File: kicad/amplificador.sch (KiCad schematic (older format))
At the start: 80 parts, among them J1 Screw_Terminal_01x01, J10 Conn_01x01_Male, J11 Conn_01x01_Male, J12 Conn_01x01_Male, J13 Conn_01x01_Male, J14 Screw_Terminal_01x01, J16 Screw_Terminal_01x01, J17 Screw_Terminal_01x01, J18 Conn_01x01_Male, J19 Conn_01x01_Male, J2 Conn_01x01_Male, J3 Conn_01x01_Male, J4 Conn_01x01_Male, J5 Conn_01x01_Male, J6 Conn_01x01_Male, J7 Screw_Terminal_01x01, J8 Screw_Terminal_01x01, J9 Conn_01x01_Male, Q1 MPSA92, Q10 MPSA42, Q11 BD135, Q12 BD136, Q13 BD135, Q14 BD136, Q15 2SD1047, Q16 2SD1047, Q17 2SB817, Q18 2SB817, Q2 MPSA42, Q3 MPSA92, Q4 MPSA42, Q5 MPSA92, Q6 MPSA92, Q7 MPSA42, Q8 MPSA92, Q9 MPSA42, U1 LM385D-1.2, U2 LM385D-1.2

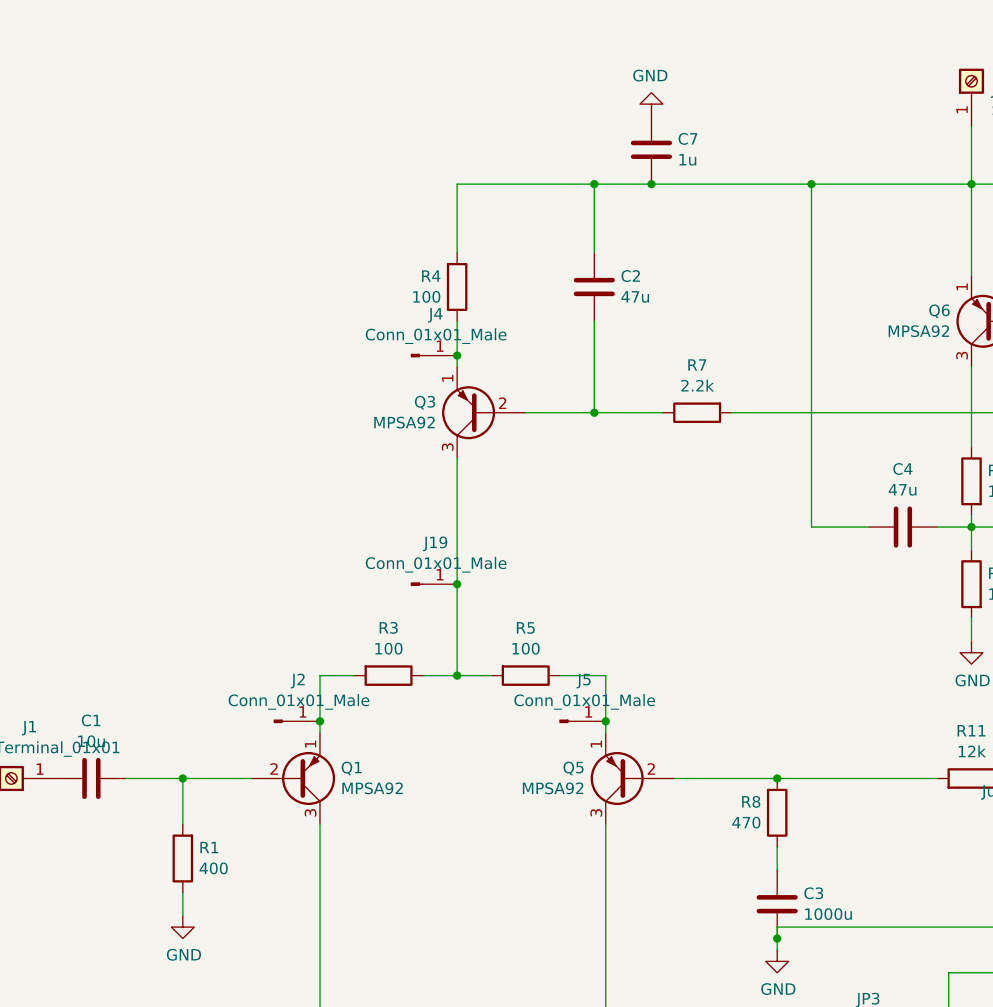
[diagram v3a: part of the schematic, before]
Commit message: PCB versión 1.0
Planos de alimentación, ancho de pistas y nuevos pines GND.
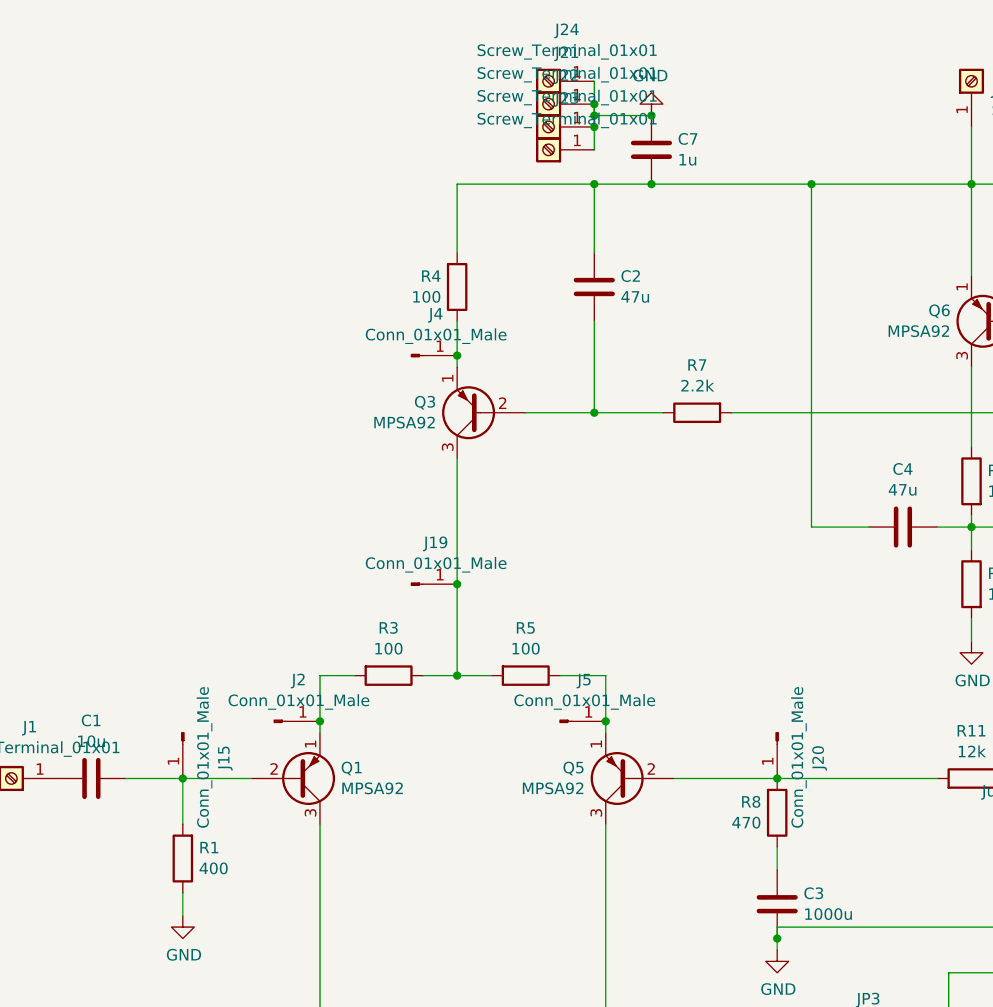
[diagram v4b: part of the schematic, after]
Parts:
- added J15, J20: Conn_01x01_Male, Connector_PinHeader_2.54mm:PinHeader_1x01_P2.54mm_Vertical, symbol Connector:Conn_01x01_Male
- added J21, J22, J23, J24: Screw_Terminal_01x01, Connector_PinHeader_2.54mm:PinHeader_1x01_P2.54mm_Vertical, symbol Connector:Screw_Terminal_01x01
- J1, J14, J16, J17, J7, J8: footprint Connector_Wire:SolderWirePad_1x01_Drill0.8mm -> Connector_PinHeader_2.54mm:PinHeader_1x01_P2.54mm_Vertical
- J10, J11, J12, J13, J18, J19, J2, J3, J4, J5, J6, J9: footprint Connector_Pin:Pin_D0.7mm_L6.5mm_W1.8mm_FlatFork -> Connector_PinHeader_2.54mm:PinHeader_1x01_P2.54mm_Vertical
- JP1, JP2, JP3, JP4: footprint kicad:SolderJumper-2_P1.3mm_Open_Pad1.0x1.5mm -> Connector_PinHeader_2.54mm:PinHeader_1x02_P2.54mm_Vertical
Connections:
- net GND: now also J21.1 (Pin_1), J22.1 (Pin_1), J23.1 (Pin_1), J24.1 (Pin_1)
- net at Q5.2 (B), R11.2, R8.2: now also J20.1 (Pin_1)
- net at C1.1, Q1.2 (B), R1.2: now also J15.1 (Pin_1)
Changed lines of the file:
@@
 F 0 "J8" V 5014 712 50  0000 R CNN
 F 1 "Screw_Terminal_01x01" V 4923 712 50  0000 R CNN
-F 2 "Connector_Wire:SolderWirePad_1x01_Drill0.8mm" H 5050 800 50  0001 C CNN
+F 2 "Connector_PinHeader_2.54mm:PinHeader_1x01_P2.54mm_Vertical" H 5050 800 50  0001 C CNN
 F 3 "~" H 5050 800 50  0001 C CNN
 	1    5050 800
@@
 F 0 "J7" V 4472 7680 50  0000 L CNN
 F 1 "Screw_Terminal_01x01" V 4563 7680 50  0000 L CNN
-F 2 "Connector_Wire:SolderWirePad_1x01_Drill0.8mm" H 4600 7600 50  0001 C CNN
+F 2 "Connector_PinHeader_2.54mm:PinHeader_1x01_P2.54mm_Vertical" H 4600 7600 50  0001 C CNN
 F 3 "~" H 4600 7600 50  0001 C CNN
 	1    4600 7600
 	0    1    1    0
-$EndComp
-$Comp
-L Connector:Screw_Terminal_01x01 J1
-U 1 1 5D1C30CA
-P 850 3850
-F 0 "J1" H 768 3625 50  0000 C CNN
-F 1 "Screw_Terminal_01x01" H 768 3716 50  0000 C CNN
-F 2 "Connector_Wire:SolderWirePad_1x01_Drill0.8mm" H 850 3850 50  0001 C CNN
-F 3 "~" H 850 3850 50  0001 C CNN
-	1    850  3850
-	-1   0    0    1
 $EndComp
 $Comp
@@
 F 0 "J16" H 10130 4842 50  0000 L CNN
 F 1 "Screw_Terminal_01x01" H 10130 4751 50  0000 L CNN
-F 2 "Connector_Wire:SolderWirePad_1x01_Drill0.8mm" H 10050 4800 50  0001 C CNN
+F 2 "Connector_PinHeader_2.54mm:PinHeader_1x01_P2.54mm_Vertical" H 10050 4800 50  0001 C CNN
 F 3 "~" H 10050 4800 50  0001 C CNN
 	1    10050 4800
@@
 F 0 "J17" H 10180 2792 50  0000 L CNN
 F 1 "Screw_Terminal_01x01" H 10180 2701 50  0000 L CNN
-F 2 "Connector_Wire:SolderWirePad_1x01_Drill0.8mm" H 10100 2750 50  0001 C CNN
+F 2 "Connector_PinHeader_2.54mm:PinHeader_1x01_P2.54mm_Vertical" H 10100 2750 50  0001 C CNN
 F 3 "~" H 10100 2750 50  0001 C CNN
 	1    10100 2750
@@
 F 0 "JP2" H 5400 4185 50  0000 C CNN
 F 1 "Jumper_NO_Small" H 5400 4094 50  0000 C CNN
-F 2 "kicad:SolderJumper-2_P1.3mm_Open_Pad1.0x1.5mm" H 5400 4000 50  0001 C CNN
+F 2 "Connector_PinHeader_2.54mm:PinHeader_1x02_P2.54mm_Vertical" H 5400 4000 50  0001 C CNN
 F 3 "~" H 5400 4000 50  0001 C CNN
 	1    5400 4000
@@
 F 0 "JP1" V 5154 4248 50  0000 L CNN
 F 1 "Jumper_NO_Small" V 5245 4248 50  0000 L CNN
-F 2 "kicad:SolderJumper-2_P1.3mm_Open_Pad1.0x1.5mm" H 5200 4200 50  0001 C CNN
+F 2 "Connector_PinHeader_2.54mm:PinHeader_1x02_P2.54mm_Vertical" H 5200 4200 50  0001 C CNN
 F 3 "~" H 5200 4200 50  0001 C CNN
 	1    5200 4200
@@
 F 0 "J3" H 2108 6081 50  0000 C CNN
 F 1 "Conn_01x01_Male" H 2108 5990 50  0000 C CNN
-F 2 "Connector_Pin:Pin_D0.7mm_L6.5mm_W1.8mm_FlatFork" H 2000 5900 50  0001 C CNN
+F 2 "Connector_PinHeader_2.54mm:PinHeader_1x01_P2.54mm_Vertical" H 2000 5900 50  0001 C CNN
 F 3 "~" H 2000 5900 50  0001 C CNN
 	1    2000 5900
@@
 F 0 "J6" H 3358 6081 50  0000 C CNN
 F 1 "Conn_01x01_Male" H 3358 5990 50  0000 C CNN
-F 2 "Connector_Pin:Pin_D0.7mm_L6.5mm_W1.8mm_FlatFork" H 3250 5900 50  0001 C CNN
+F 2 "Connector_PinHeader_2.54mm:PinHeader_1x01_P2.54mm_Vertical" H 3250 5900 50  0001 C CNN
 F 3 "~" H 3250 5900 50  0001 C CNN
 	1    3250 5900
@@
 F 0 "J4" H 2708 2181 50  0000 C CNN
 F 1 "Conn_01x01_Male" H 2708 2090 50  0000 C CNN
-F 2 "Connector_Pin:Pin_D0.7mm_L6.5mm_W1.8mm_FlatFork" H 2600 2000 50  0001 C CNN
+F 2 "Connector_PinHeader_2.54mm:PinHeader_1x01_P2.54mm_Vertical" H 2600 2000 50  0001 C CNN
 F 3 "~" H 2600 2000 50  0001 C CNN
 	1    2600 2000
@@
 F 0 "J2" H 2108 3781 50  0000 C CNN
 F 1 "Conn_01x01_Male" H 2108 3690 50  0000 C CNN
-F 2 "Connector_Pin:Pin_D0.7mm_L6.5mm_W1.8mm_FlatFork" H 2000 3600 50  0001 C CNN
+F 2 "Connector_PinHeader_2.54mm:PinHeader_1x01_P2.54mm_Vertical" H 2000 3600 50  0001 C CNN
 F 3 "~" H 2000 3600 50  0001 C CNN
 	1    2000 3600
@@
 F 0 "J5" H 3358 3781 50  0000 C CNN
 F 1 "Conn_01x01_Male" H 3358 3690 50  0000 C CNN
-F 2 "Connector_Pin:Pin_D0.7mm_L6.5mm_W1.8mm_FlatFork" H 3250 3600 50  0001 C CNN
+F 2 "Connector_PinHeader_2.54mm:PinHeader_1x01_P2.54mm_Vertical" H 3250 3600 50  0001 C CNN
 F 3 "~" H 3250 3600 50  0001 C CNN
 	1    3250 3600
@@
 F 0 "J9" H 6358 1931 50  0000 C CNN
 F 1 "Conn_01x01_Male" H 6358 1840 50  0000 C CNN
-F 2 "Connector_Pin:Pin_D0.7mm_L6.5mm_W1.8mm_FlatFork" H 6250 1750 50  0001 C CNN
+F 2 "Connector_PinHeader_2.54mm:PinHeader_1x01_P2.54mm_Vertical" H 6250 1750 50  0001 C CNN
 F 3 "~" H 6250 1750 50  0001 C CNN
 	1    6250 1750
@@
 F 0 "J10" V 7962 3144 50  0000 L CNN
 F 1 "Conn_01x01_Male" V 8053 3144 50  0000 L CNN
-F 2 "Connector_Pin:Pin_D0.7mm_L6.5mm_W1.8mm_FlatFork" H 7900 3100 50  0001 C CNN
+F 2 "Connector_PinHeader_2.54mm:PinHeader_1x01_P2.54mm_Vertical" H 7900 3100 50  0001 C CNN
 F 3 "~" H 7900 3100 50  0001 C CNN
 	1    7900 3100
@@
 F 0 "J11" V 7962 4544 50  0000 L CNN
 F 1 "Conn_01x01_Male" V 8053 4544 50  0000 L CNN
-F 2 "Connector_Pin:Pin_D0.7mm_L6.5mm_W1.8mm_FlatFork" H 7900 4500 50  0001 C CNN
+F 2 "Connector_PinHeader_2.54mm:PinHeader_1x01_P2.54mm_Vertical" H 7900 4500 50  0001 C CNN
 F 3 "~" H 7900 4500 50  0001 C CNN
 	1    7900 4500
@@
 F 0 "J13" H 8358 4531 50  0000 C CNN
 F 1 "Conn_01x01_Male" H 8358 4440 50  0000 C CNN
-F 2 "Connector_Pin:Pin_D0.7mm_L6.5mm_W1.8mm_FlatFork" H 8250 4350 50  0001 C CNN
+F 2 "Connector_PinHeader_2.54mm:PinHeader_1x01_P2.54mm_Vertical" H 8250 4350 50  0001 C CNN
 F 3 "~" H 8250 4350 50  0001 C CNN
 	1    8250 4350
@@
 F 0 "J12" H 8358 3831 50  0000 C CNN
 F 1 "Conn_01x01_Male" H 8358 3740 50  0000 C CNN
-F 2 "Connector_Pin:Pin_D0.7mm_L6.5mm_W1.8mm_FlatFork" H 8250 3650 50  0001 C CNN
+F 2 "Connector_PinHeader_2.54mm:PinHeader_1x01_P2.54mm_Vertical" H 8250 3650 50  0001 C CNN
 F 3 "~" H 8250 3650 50  0001 C CNN
 	1    8250 3650
@@
 F 0 "J18" H 6758 5431 50  0000 C CNN
 F 1 "Conn_01x01_Male" H 6758 5340 50  0000 C CNN
-F 2 "Connector_Pin:Pin_D0.7mm_L6.5mm_W1.8mm_FlatFork" H 6650 5250 50  0001 C CNN
+F 2 "Connector_PinHeader_2.54mm:PinHeader_1x01_P2.54mm_Vertical" H 6650 5250 50  0001 C CNN
 F 3 "~" H 6650 5250 50  0001 C CNN
 	1    6650 5250
@@
 F 0 "JP3" H 4600 5185 50  0000 C CNN
 F 1 "Jumper_NO_Small" H 4600 5094 50  0000 C CNN
-F 2 "kicad:SolderJumper-2_P1.3mm_Open_Pad1.0x1.5mm" H 4600 5000 50  0001 C CNN
+F 2 "Connector_PinHeader_2.54mm:PinHeader_1x02_P2.54mm_Vertical" H 4600 5000 50  0001 C CNN
 F 3 "~" H 4600 5000 50  0001 C CNN
 	1    4600 5000
@@
 F 0 "JP4" H 6000 2685 50  0000 C CNN
 F 1 "Jumper_NO_Small" H 6000 2594 50  0000 C CNN
-F 2 "kicad:SolderJumper-2_P1.3mm_Open_Pad1.0x1.5mm" H 6000 2500 50  0001 C CNN
+F 2 "Connector_PinHeader_2.54mm:PinHeader_1x02_P2.54mm_Vertical" H 6000 2500 50  0001 C CNN
 F 3 "~" H 6000 2500 50  0001 C CNN
 	1    6000 2500
@@
 F 0 "J19" H 2708 3181 50  0000 C CNN
 F 1 "Conn_01x01_Male" H 2708 3090 50  0000 C CNN
-F 2 "Connector_Pin:Pin_D0.7mm_L6.5mm_W1.8mm_FlatFork" H 2600 3000 50  0001 C CNN
+F 2 "Connector_PinHeader_2.54mm:PinHeader_1x01_P2.54mm_Vertical" H 2600 3000 50  0001 C CNN
 F 3 "~" H 2600 3000 50  0001 C CNN
 	1    2600 3000
@@
 F 0 "J14" H 9930 4042 50  0000 L CNN
 F 1 "Screw_Terminal_01x01" H 9930 3951 50  0000 L CNN
-F 2 "Connector_Wire:SolderWirePad_1x01_Drill0.8mm" H 9850 4000 50  0001 C CNN
+F 2 "Connector_PinHeader_2.54mm:PinHeader_1x01_P2.54mm_Vertical" H 9850 4000 50  0001 C CNN
 F 3 "~" H 9850 4000 50  0001 C CNN
 	1    9850 4000
@@
 Wire Wire Line
 	9650 4000 9250 4000
+$Comp
+L Connector:Conn_01x01_Male J15
+U 1 1 5D31F6CD
+P 1600 3650
+F 0 "J15" H 1708 3831 50  0000 C CNN
+F 1 "Conn_01x01_Male" H 1708 3740 50  0000 C CNN
+F 2 "Connector_PinHeader_2.54mm:PinHeader_1x01_P2.54mm_Vertical" H 1600 3650 50  0001 C CNN
+F 3 "~" H 1600 3650 50  0001 C CNN
+	1    1600 3650
+	0    1    1    0
+$EndComp
+$Comp
+L Connector:Screw_Terminal_01x01 J1
+U 1 1 5D1C30CA
+P 850 3850
+F 0 "J1" H 768 3625 50  0000 C CNN
+F 1 "Screw_Terminal_01x01" H 768 3716 50  0000 C CNN
+F 2 "Connector_PinHeader_2.54mm:PinHeader_1x01_P2.54mm_Vertical" H 850 3850 50  0001 C CNN
+F 3 "~" H 850 3850 50  0001 C CNN
+	1    850  3850
+	-1   0    0    1
+$EndComp
+$Comp
+L Connector:Conn_01x01_Male J20
+U 1 1 5D31FA4D
+P 4200 3650
+F 0 "J20" H 4308 3831 50  0000 C CNN
+F 1 "Conn_01x01_Male" H 4308 3740 50  0000 C CNN
+F 2 "Connector_PinHeader_2.54mm:PinHeader_1x01_P2.54mm_Vertical" H 4200 3650 50  0001 C CNN
+F 3 "~" H 4200 3650 50  0001 C CNN
+	1    4200 3650
+	0    1    1    0
+$EndComp
+$Comp
+L Connector:Screw_Terminal_01x01 J22
+U 1 1 5D33116F
+P 3200 1000
+F 0 "J22" H 3118 775 50  0000 C CNN
+F 1 "Screw_Terminal_01x01" H 3118 866 50  0000 C CNN
+F 2 "Connector_PinHeader_2.54mm:PinHeader_1x01_P2.54mm_Vertical" H 3200 1000 50  0001 C CNN
+F 3 "~" H 3200 1000 50  0001 C CNN
+	1    3200 1000
+	-1   0    0    1
+$EndComp
+$Comp
+L Connector:Screw_Terminal_01x01 J21
+U 1 1 5D339AF8
+P 3200 900
+F 0 "J21" H 3118 675 50  0000 C CNN
+F 1 "Screw_Terminal_01x01" H 3118 766 50  0000 C CNN
+F 2 "Connector_PinHeader_2.54mm:PinHeader_1x01_P2.54mm_Vertical" H 3200 900 50  0001 C CNN
+F 3 "~" H 3200 900 50  0001 C CNN
+	1    3200 900
+	-1   0    0    1
+$EndComp
+$Comp
+L Connector:Screw_Terminal_01x01 J23
+U 1 1 5D342184
+P 3200 1100
+F 0 "J23" H 3118 875 50  0000 C CNN
+F 1 "Screw_Terminal_01x01" H 3118 966 50  0000 C CNN
+F 2 "Connector_PinHeader_2.54mm:PinHeader_1x01_P2.54mm_Vertical" H 3200 1100 50  0001 C CNN
+F 3 "~" H 3200 1100 50  0001 C CNN
+	1    3200 1100
+	-1   0    0    1
+$EndComp
+Wire Wire Line
+	3400 950  3400 1000
+Connection ~ 3400 1000
+Wire Wire Line
+	3400 1000 3400 1100
+Connection ~ 3400 950
+Wire Wire Line
+	3400 950  3400 900
+Wire Wire Line
+	3400 950  3650 950
+Connection ~ 3650 950
+$Comp
+L Connector:Screw_Terminal_01x01 J24
+U 1 1 5D3671E0
+P 3200 800
+F 0 "J24" H 3118 575 50  0000 C CNN
+F 1 "Screw_Terminal_01x01" H 3118 666 50  0000 C CNN
+F 2 "Connector_PinHeader_2.54mm:PinHeader_1x01_P2.54mm_Vertical" H 3200 800 50  0001 C CNN
+F 3 "~" H 3200 800 50  0001 C CNN
+	1    3200 800
+	-1   0    0    1
+$EndComp
+Wire Wire Line
+	3400 800  3400 900
+Connection ~ 3400 900
+Wire Wire Line
+	3400 900  3400 950
 $EndSCHEMATC
